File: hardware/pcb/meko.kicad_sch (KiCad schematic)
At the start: 0 parts

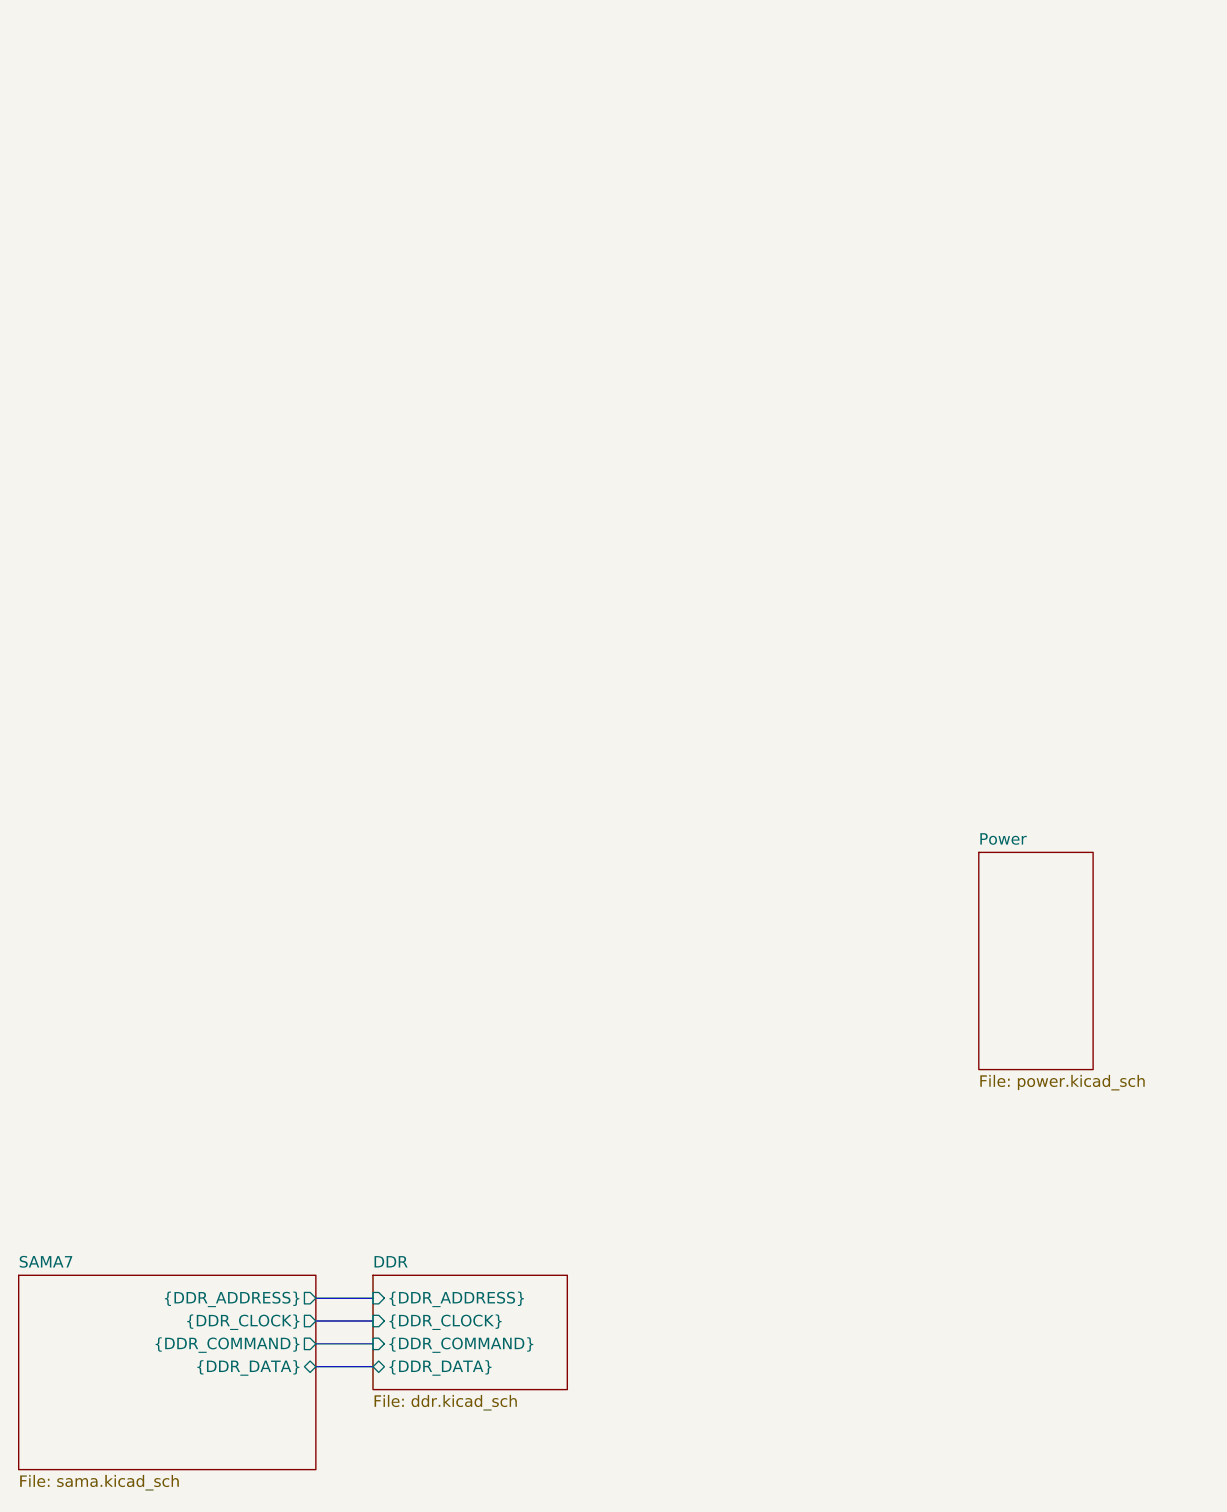
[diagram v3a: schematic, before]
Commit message: added maya-w3, made symbol
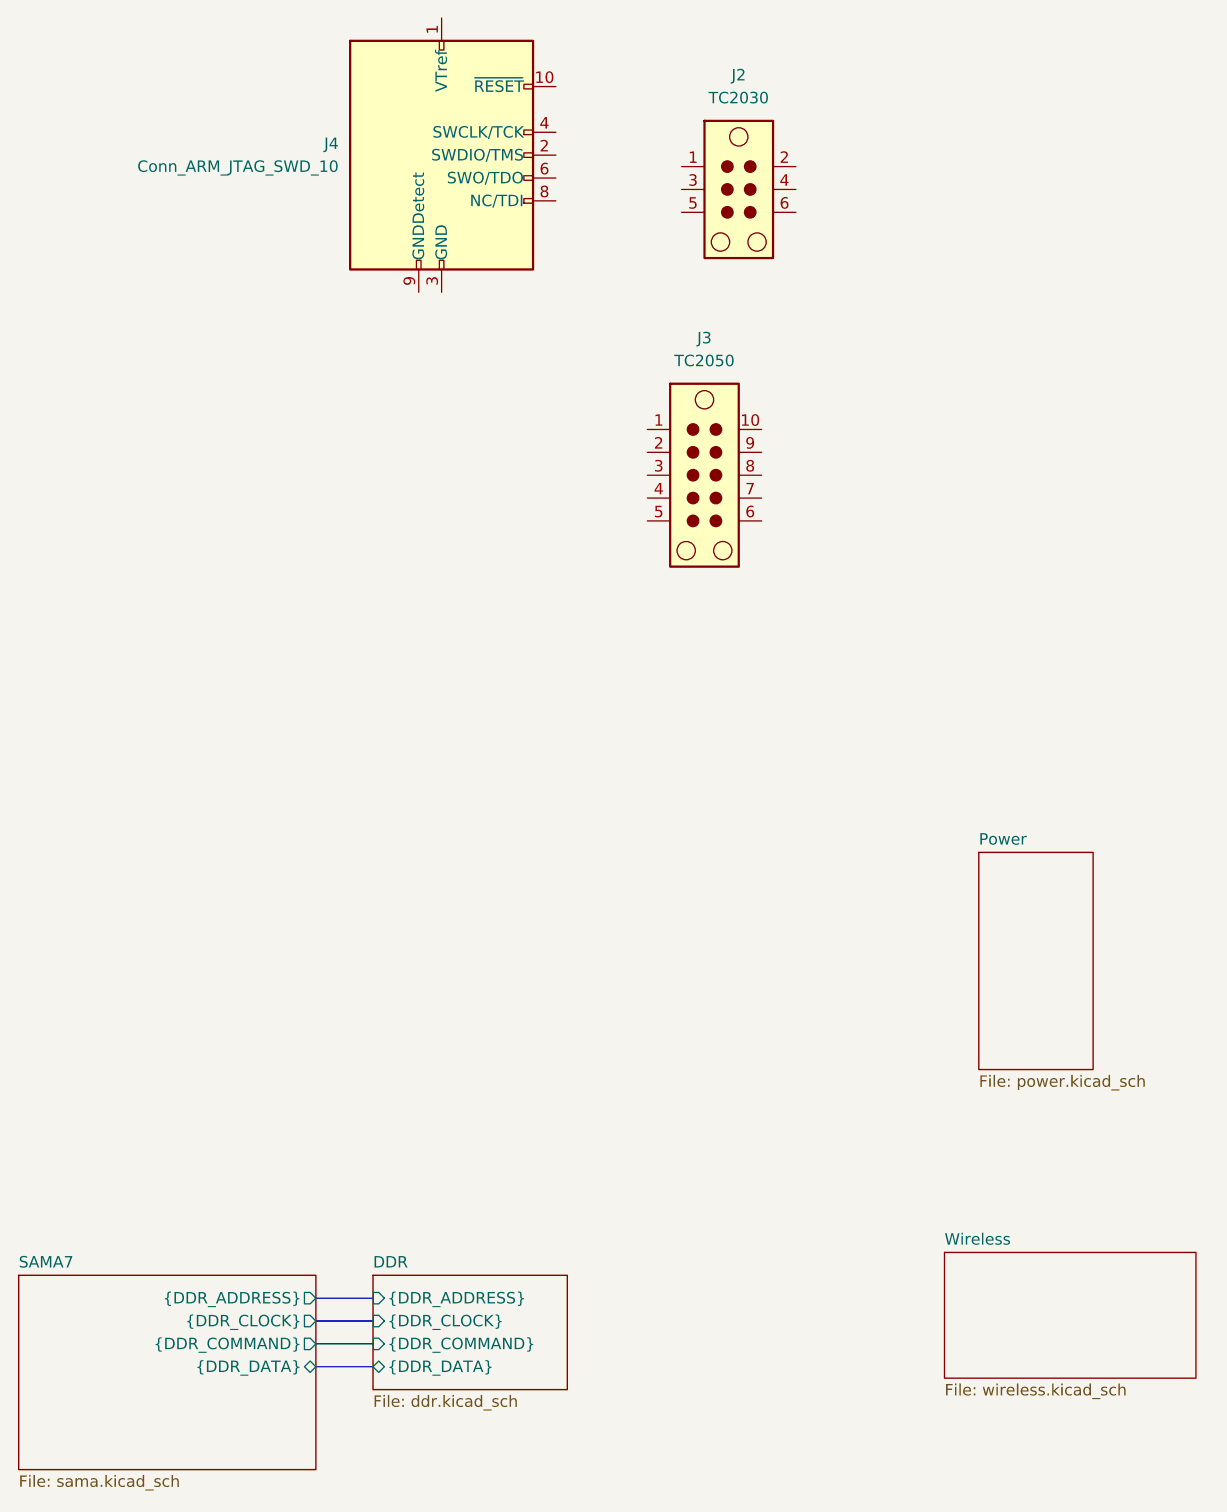
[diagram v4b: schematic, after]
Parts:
- added J2: TC2030, Connector:Tag-Connect_TC2030-IDC-NL_2x03_P1.27mm_Vertical, symbol Connector:TC2030
- added J3: TC2050, Connector:Tag-Connect_TC2050-IDC-NL_2x05_P1.27mm_Vertical, symbol Connector:TC2050
- added J4: Conn_ARM_JTAG_SWD_10, Connector_PinHeader_1.27mm:PinHeader_2x05_P1.27mm_Vertical_SMD, symbol Connector:Conn_ARM_JTAG_SWD_10
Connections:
- new net: J4.3 (GND), J4.5 (GND)
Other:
- added sheet Wireless (wireless.kicad_sch)

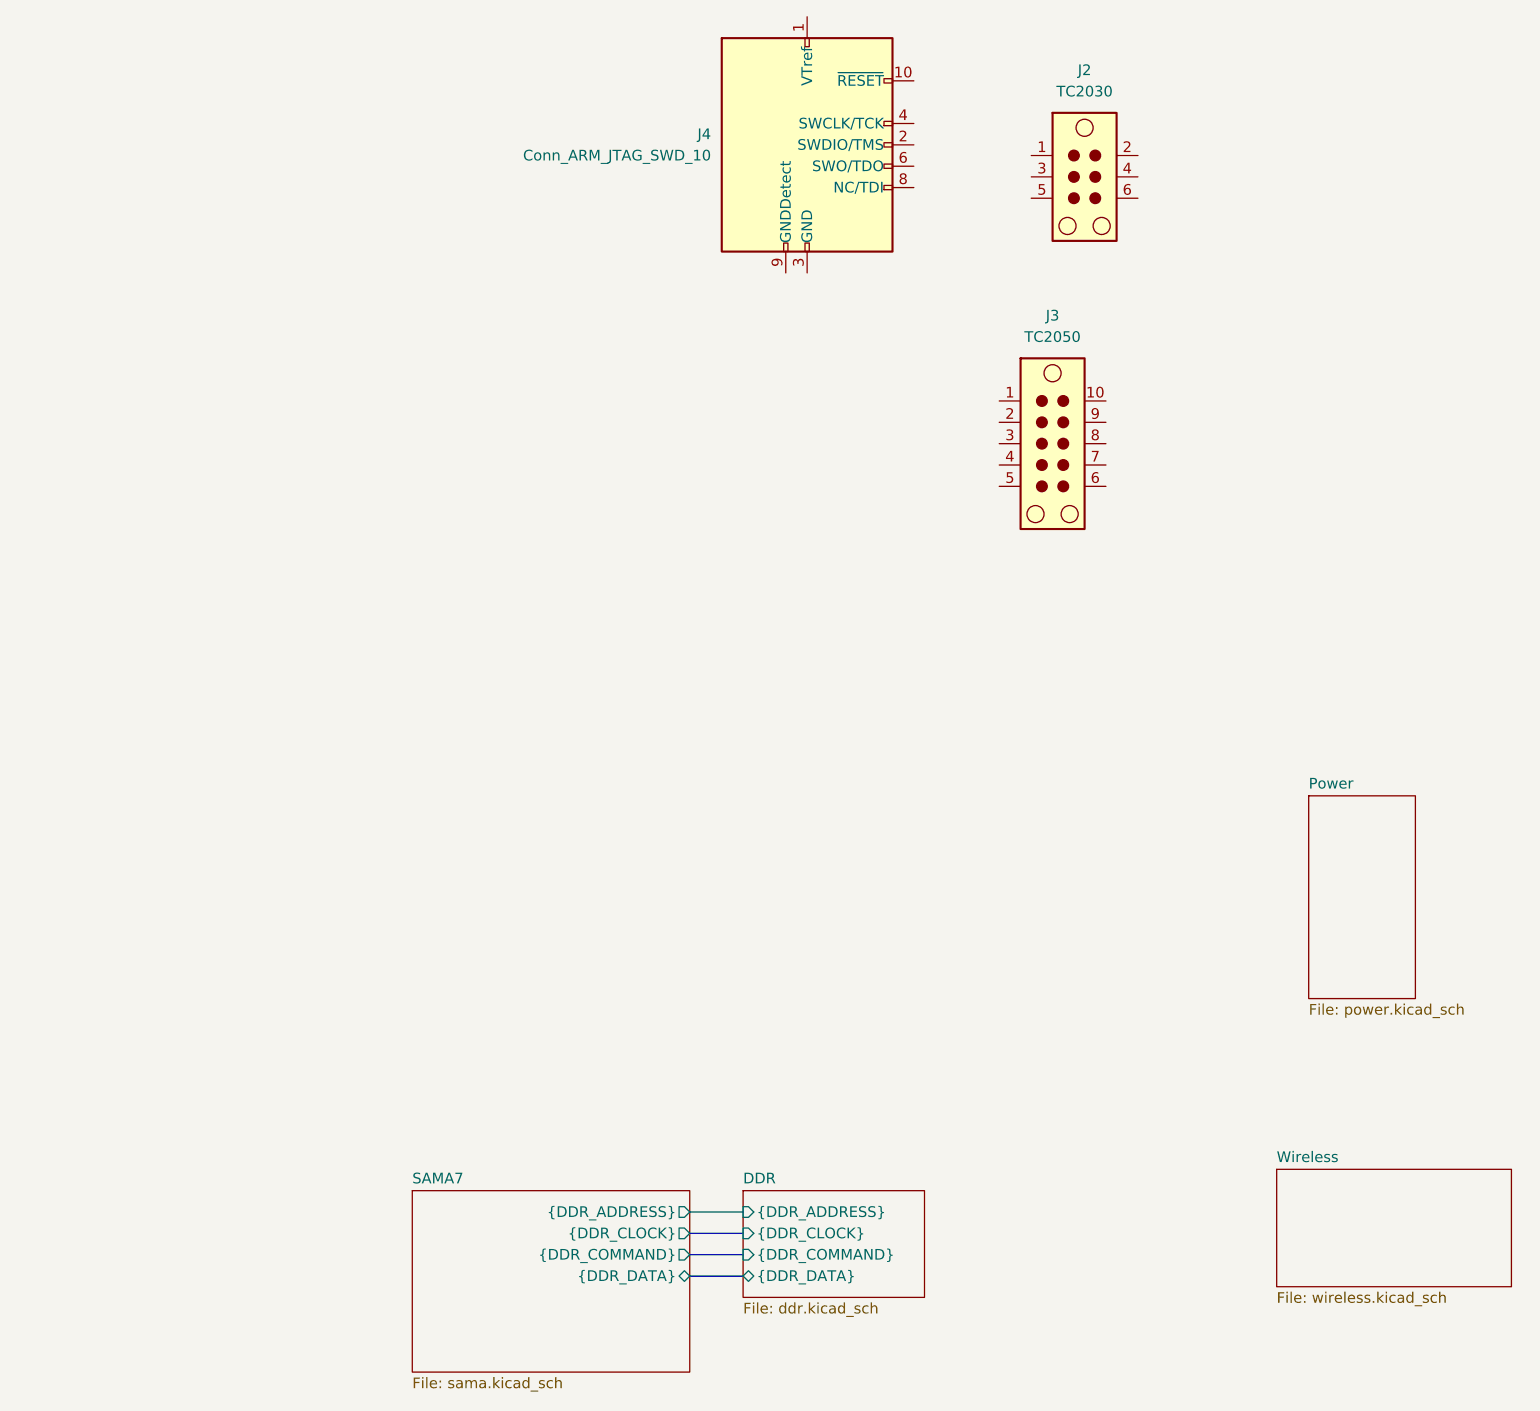
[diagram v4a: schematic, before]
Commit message: started usb
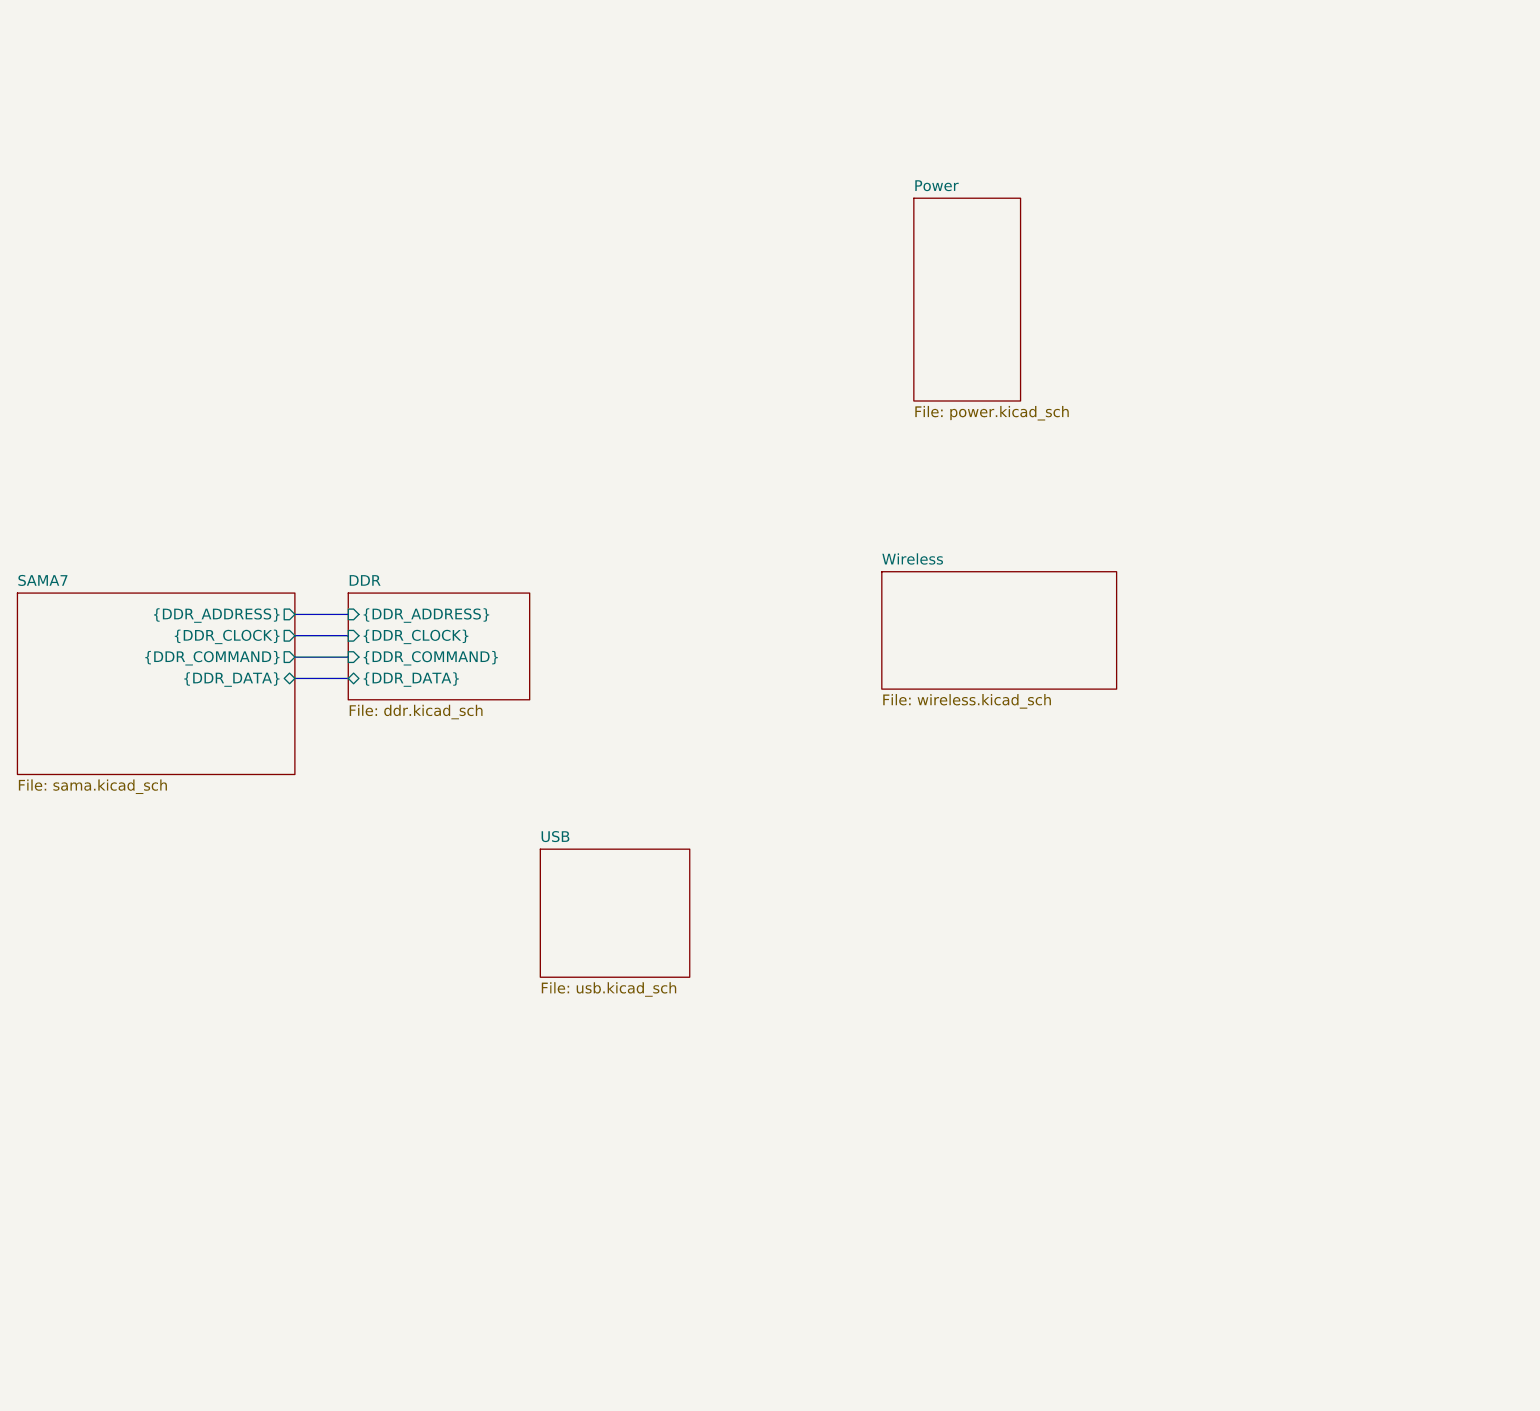
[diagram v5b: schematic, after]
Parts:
- removed J2: TC2030, Connector:Tag-Connect_TC2030-IDC-NL_2x03_P1.27mm_Vertical, symbol Connector:TC2030
- removed J3: TC2050, Connector:Tag-Connect_TC2050-IDC-NL_2x05_P1.27mm_Vertical, symbol Connector:TC2050
- removed J4: Conn_ARM_JTAG_SWD_10, Connector_PinHeader_1.27mm:PinHeader_2x05_P1.27mm_Vertical_SMD, symbol Connector:Conn_ARM_JTAG_SWD_10
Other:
- added sheet USB (usb.kicad_sch)

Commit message: contiunued working
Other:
- added sheet Buttons (buttons.kicad_sch)
- added sheet DAC (dac.kicad_sch)
- added sheet Display (display.kicad_sch)
- added sheet SD Cards (sd.kicad_sch)
- added sheet Touch Pad (touch_pad.kicad_sch)
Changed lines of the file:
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@@
+	)
+	(sheet
+		(at 196.85 146.05)
+		(size 25.4 12.7)
+		(exclude_from_sim no)
+		(in_bom yes)
+		(on_board yes)
+		(dnp no)
+		(fields_autoplaced yes)
+		(stroke
+			(width 0.1524)
+			(type solid)
+		)
+		(fill
+			(color 0 0 0 0)
+		)
+		(property "Sheetname" "Display"
+			(at 196.85 145.3384 0)
+			(show_name no)
+			(do_not_autoplace no)
+			(effects
+				(font
+					(size 1.27 1.27)
+				)
+				(justify left bottom)
+			)
+		)
+		(property "Sheetfile" "display.kicad_sch"
+			(at 196.85 159.3346 0)
+			(show_name no)
+			(do_not_autoplace no)
+			(effects
+				(font
+					(size 1.27 1.27)
+				)
+				(justify left top)
+			)
+		)
+		(instances
+			(project "meko"
+				(path "/da54f10a-146b-4941-a9c7-55c7173bb101"
+					(page "9")
+				)
+			)
+		)
 	)
 	(sheet
@@
 	)
 	(sheet
+		(at 149.86 157.48)
+		(size 19.05 10.16)
+		(exclude_from_sim no)
+		(in_bom yes)
+		(on_board yes)
+		(dnp no)
+		(fields_autoplaced yes)
+		(stroke
+			(width 0.1524)
+			(type solid)
+		)
+		(fill
+			(color 0 0 0 0)
+		)
+		(property "Sheetname" "SD Cards"
+			(at 149.86 156.7684 0)
+			(show_name no)
+			(do_not_autoplace no)
+			(effects
+				(font
+					(size 1.27 1.27)
+				)
+				(justify left bottom)
+			)
+		)
+		(property "Sheetfile" "sd.kicad_sch"
+			(at 149.86 168.2246 0)
+			(show_name no)
+			(do_not_autoplace no)
+			(effects
+				(font
+					(size 1.27 1.27)
+				)
+				(justify left top)
+			)
+		)
+		(instances
+			(project "meko"
+				(path "/da54f10a-146b-4941-a9c7-55c7173bb101"
+					(page "8")
+				)
+			)
+		)
+	)
+	(sheet
 		(at 173.99 53.34)
 		(size 12.7 24.13)
@@
 	)
 	(sheet
+		(at 214.63 120.65)
+		(size 30.48 15.24)
+		(exclude_from_sim no)
+		(in_bom yes)
+		(on_board yes)
+		(dnp no)
+		(fields_autoplaced yes)
+		(stroke
+			(width 0.1524)
+			(type solid)
+		)
+		(fill
+			(color 0 0 0 0)
+		)
+		(property "Sheetname" "Touch Pad"
+			(at 214.63 119.9384 0)
+			(show_name no)
+			(do_not_autoplace no)
+			(effects
+				(font
+					(size 1.27 1.27)
+				)
+				(justify left bottom)
+			)
+		)
+		(property "Sheetfile" "touch_pad.kicad_sch"
+			(at 214.63 136.4746 0)
+			(show_name no)
+			(do_not_autoplace no)
+			(effects
+				(font
+					(size 1.27 1.27)
+				)
+				(justify left top)
+			)
+		)
+		(instances
+			(project "meko"
+				(path "/da54f10a-146b-4941-a9c7-55c7173bb101"
+					(page "10")
+				)
+			)
+		)
+	)
+	(sheet
 		(at 170.18 97.79)
 		(size 27.94 13.97)
@@
 				)
 			)
+		)
+	)
+	(sheet
+		(at 113.03 168.91)
+		(size 12.7 3.81)
+		(exclude_from_sim no)
+		(in_bom yes)
+		(on_board yes)
+		(dnp no)
+		(fields_autoplaced yes)
+		(stroke
+			(width 0.1524)
+			(type solid)
+		)
+		(fill
+			(color 0 0 0 0)
+		)
+		(property "Sheetname" "Buttons"
+			(at 113.03 168.1984 0)
+			(show_name no)
+			(do_not_autoplace no)
+			(effects
+				(font
+					(size 1.27 1.27)
+				)
+				(justify left bottom)
+			)
+		)
+		(property "Sheetfile" "buttons.kicad_sch"
+			(at 113.03 173.3046 0)
+			(show_name no)
+			(do_not_autoplace no)
+			(effects
+				(font
+					(size 1.27 1.27)
+				)
+				(justify left top)
+			)
+		)
+		(instances
+			(project "meko"
+				(path "/da54f10a-146b-4941-a9c7-55c7173bb101"
+					(page "11")
+				)
+			)
+		)
+	)
+	(sheet
+		(at 88.9 148.59)
+		(size 20.32 15.24)
+		(exclude_from_sim no)
+		(in_bom yes)
+		(on_board yes)
+		(dnp no)
+		(fields_autoplaced yes)
+		(stroke
+			(width 0.1524)
+			(type solid)
+		)
+		(fill
+			(color 0 0 0 0)
+		)
+		(property "Sheetname" "DAC"
+			(at 88.9 147.8784 0)
+			(show_name no)
+			(do_not_autoplace no)
+			(effects
+				(font
+					(size 1.27 1.27)
+				)
+				(justify left bottom)
+			)
+		)
+		(property "Sheetfile" "dac.kicad_sch"
+			(at 88.9 164.4146 0)
+			(show_name no)
+			(do_not_autoplace no)
+			(effects
+				(font
+					(size 1.27 1.27)
+				)
+				(justify left top)
+			)
+		)
+		(instances
+			(project "meko"
+				(path "/da54f10a-146b-4941-a9c7-55c7173bb101"
+					(page "7")
+				)
+			)
